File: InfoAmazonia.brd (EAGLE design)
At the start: 103.5 x 75.6 mm, 83 parts, among them IC1 ADAFRUIT FONA, IC10 TL032C, IC11 NE555, IC12 CA3140AM Z, IC13 TL081BCDG4, IC2 LM2662, IC3 74HC4051, IC4 MIC29302AWD, IC5 4050D, IC6 4053D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

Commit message: - Mudado o codigo de alguns componentes para bater com o BOM
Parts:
- IC3: value 74HC4051 -> HEF4051BT
- IC5: value 4050D -> CD4050BD
- IC6, IC7, IC8: value 4053D -> 74HC4053D
- J1, J2, J3: value BNCPTH -> 31-5431-10RFX
- JP1: value ANALOG -> 89400-0420
- JP2: value SERIAL -> 89400-0420
- JP3: value I2C -> 89400-0420
- JP4: value PWM -> 89400-0420
- MD4, MD6: value (none) -> INFO-AMAZONIA-MODULE
- R3: value 43 -> 100
- R4: value 100 -> 220
- U3: value USD-SOCKETNEW -> 10100660686
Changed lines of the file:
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@@
 <?xml version="1.0" encoding="utf-8"?>
 <!DOCTYPE eagle SYSTEM "eagle.dtd">
-<eagle version="7.3.0">
+<eagle version="7.2.0">
 <drawing>
 <settings>
@@
 </element>
 <element name="IC9" library="InfoAmazonia" package="SHT2X" value="SHT20" x="92.075" y="38.1" smashed="yes" rot="R90"/>
-<element name="J1" library="InfoAmazonia" package="BNC" value="BNCPTH" x="40.64" y="35.56" smashed="yes">
+<element name="J1" library="InfoAmazonia" package="BNC" value="31-5431-10RFX" x="40.64" y="35.56" smashed="yes">
 <attribute name="VALUE" x="34.29" y="43.18" size="0.4064" layer="27" font="vector" ratio="15" rot="SR0"/>
 </element>
@@
 <attribute name="VALUE" x="17.145" y="14.605" size="1.27" layer="27" font="vector" ratio="15" rot="R90"/>
 </element>
-<element name="R4" library="InfoAmazonia" package="R0603" value="100" x="13.97" y="10.16" smashed="yes">
+<element name="R4" library="InfoAmazonia" package="R0603" value="220" x="13.97" y="10.16" smashed="yes">
 <attribute name="NAME" x="12.85875" y="10.95375" size="1.27" layer="25" font="vector" ratio="15"/>
 <attribute name="VALUE" x="13.335" y="8.255" size="1.27" layer="27" font="vector" ratio="15"/>
 </element>
-<element name="R3" library="InfoAmazonia" package="R0603" value="43" x="10.16" y="10.16" smashed="yes">
+<element name="R3" library="InfoAmazonia" package="R0603" value="100" x="10.16" y="10.16" smashed="yes">
 <attribute name="NAME" x="9.2075" y="10.95375" size="1.27" layer="25" font="vector" ratio="15"/>
 <attribute name="VALUE" x="9.525" y="8.255" size="1.27" layer="27" font="vector" ratio="15"/>
@@
 <attribute name="VALUE" x="26.67" y="22.225" size="1.016" layer="27" font="vector" ratio="15"/>
 </element>
-<element name="U3" library="InfoAmazonia" package="MICRO-SD-SOCKET-PP" value="USD-SOCKETNEW" x="16.51" y="43.18" smashed="yes" rot="R90">
+<element name="U3" library="InfoAmazonia" package="MICRO-SD-SOCKET-PP" value="10100660686" x="16.51" y="43.18" smashed="yes" rot="R90">
 <attribute name="NAME" x="12.7" y="37.62375" size="1.778" layer="25" font="vector" ratio="15" rot="SR270"/>
 <attribute name="VALUE" x="11.43" y="34.29" size="0.8128" layer="27" font="vector" ratio="15" rot="R90"/>
 </element>
-<element name="IC5" library="InfoAmazonia" package="SO16" value="4050D" x="24.13" y="34.925" smashed="yes" rot="R270">
+<element name="IC5" library="InfoAmazonia" package="SO16" value="CD4050BD" x="24.13" y="34.925" smashed="yes" rot="R270">
 <attribute name="VALUE" x="23.495" y="38.989" size="1.27" layer="27" font="vector" ratio="15" rot="R270"/>
 <attribute name="NAME" x="24.765" y="33.655" size="1.27" layer="25" font="vector" ratio="15" rot="R90"/>
@@
 <attribute name="VALUE" x="80.645" y="71.755" size="1.27" layer="27" font="vector" ratio="15"/>
 </element>
-<element name="JP1" library="InfoAmazonia" package="JST-4-PTH-VERT" value="ANALOG" x="99.06" y="9.525" smashed="yes" rot="R270">
+<element name="JP1" library="InfoAmazonia" package="JST-4-PTH-VERT" value="89400-0420" x="99.06" y="9.525" smashed="yes" rot="R270">
 <attribute name="VALUE" x="102.06" y="8.525" size="0.4064" layer="27" rot="R270"/>
 </element>
-<element name="JP3" library="InfoAmazonia" package="JST-4-PTH-VERT" value="I2C" x="99.06" y="43.815" smashed="yes" rot="R270">
+<element name="JP3" library="InfoAmazonia" package="JST-4-PTH-VERT" value="89400-0420" x="99.06" y="43.815" smashed="yes" rot="R270">
 <attribute name="VALUE" x="102.06" y="42.815" size="0.4064" layer="27" rot="R270"/>
 </element>
-<element name="JP2" library="InfoAmazonia" package="JST-4-PTH-VERT" value="SERIAL" x="99.06" y="32.385" smashed="yes" rot="R270">
+<element name="JP2" library="InfoAmazonia" package="JST-4-PTH-VERT" value="89400-0420" x="99.06" y="32.385" smashed="yes" rot="R270">
 <attribute name="VALUE" x="102.06" y="31.385" size="0.4064" layer="27" rot="R270"/>
 </element>
-<element name="JP4" library="InfoAmazonia" package="JST-4-PTH-VERT" value="PWM" x="99.06" y="20.955" smashed="yes" rot="R270">
+<element name="JP4" library="InfoAmazonia" package="JST-4-PTH-VERT" value="89400-0420" x="99.06" y="20.955" smashed="yes" rot="R270">
 <attribute name="VALUE" x="102.06" y="19.955" size="0.4064" layer="27" rot="R270"/>
 </element>
 <element name="MD1" library="InfoAmazonia" package="INFO-AMAZONIA-MODULE" value="INFO-AMAZONIA-MODULE" x="40.64" y="20.32" rot="R270"/>
-<element name="J2" library="InfoAmazonia" package="BNC" value="BNCPTH" x="57.785" y="35.56" smashed="yes">
+<element name="J2" library="InfoAmazonia" package="BNC" value="31-5431-10RFX" x="57.785" y="35.56" smashed="yes">
 <attribute name="VALUE" x="51.435" y="43.18" size="0.4064" layer="27" rot="SR0"/>
 </element>
-<element name="J3" library="InfoAmazonia" package="BNC" value="BNCPTH" x="74.93" y="35.56" smashed="yes">
+<element name="J3" library="InfoAmazonia" package="BNC" value="31-5431-10RFX" x="74.93" y="35.56" smashed="yes">
 <attribute name="VALUE" x="68.58" y="43.18" size="0.4064" layer="27" rot="SR0"/>
 </element>
-<element name="MD4" library="InfoAmazonia" package="INFO-AMAZONIA-MODULE" value="" x="48.26" y="66.04"/>
-<element name="MD6" library="InfoAmazonia" package="INFO-AMAZONIA-MODULE" value="" x="17.78" y="66.04"/>
+<element name="MD4" library="InfoAmazonia" package="INFO-AMAZONIA-MODULE" value="INFO-AMAZONIA-MODULE" x="48.26" y="66.04"/>
+<element name="MD6" library="InfoAmazonia" package="INFO-AMAZONIA-MODULE" value="INFO-AMAZONIA-MODULE" x="17.78" y="66.04"/>
 <element name="MD5" library="InfoAmazonia" package="INFO-AMAZONIA-MODULE" value="INFO-AMAZONIA-MODULE" x="78.74" y="66.04"/>
-<element name="IC3" library="InfoAmazonia" package="SO16" value="74HC4051" x="73.025" y="18.415" smashed="yes" rot="R90">
+<element name="IC3" library="InfoAmazonia" package="SO16" value="HEF4051BT" x="73.025" y="18.415" smashed="yes" rot="R90">
 <attribute name="NAME" x="73.66" y="17.145" size="1.27" layer="25" font="vector" ratio="15" rot="R90"/>
 <attribute name="VALUE" x="75.1078" y="22.6187" size="1.016" layer="27" ratio="10" rot="R180"/>
@@
 <attribute name="VALUE" x="95.25" y="46.99" size="1.27" layer="27" rot="R90"/>
 </element>
-<element name="IC6" library="InfoAmazonia" package="SO16" value="4053D" x="38.735" y="18.415" smashed="yes" rot="R90">
+<element name="IC6" library="InfoAmazonia" package="SO16" value="74HC4053D" x="38.735" y="18.415" smashed="yes" rot="R90">
 <attribute name="VALUE" x="39.37" y="14.351" size="1.27" layer="27" ratio="10" rot="R90"/>
 <attribute name="NAME" x="39.37" y="17.145" size="1.27" layer="25" font="vector" ratio="15" rot="R90"/>
 </element>
 <element name="MD2" library="InfoAmazonia" package="INFO-AMAZONIA-MODULE" value="INFO-AMAZONIA-MODULE" x="57.785" y="20.32" rot="R270"/>
-<element name="IC7" library="InfoAmazonia" package="SO16" value="4053D" x="50.165" y="18.415" smashed="yes" rot="R90">
+<element name="IC7" library="InfoAmazonia" package="SO16" value="74HC4053D" x="50.165" y="18.415" smashed="yes" rot="R90">
 <attribute name="VALUE" x="50.8" y="14.351" size="1.27" layer="27" ratio="10" rot="R90"/>
 <attribute name="NAME" x="50.8" y="17.145" size="1.27" layer="25" font="vector" ratio="15" rot="R90"/>
 </element>
 <element name="MD3" library="InfoAmazonia" package="INFO-AMAZONIA-MODULE" value="INFO-AMAZONIA-MODULE" x="74.93" y="20.32" rot="R270"/>
-<element name="IC8" library="InfoAmazonia" package="SO16" value="4053D" x="61.595" y="18.415" smashed="yes" rot="R90">
+<element name="IC8" library="InfoAmazonia" package="SO16" value="74HC4053D" x="61.595" y="18.415" smashed="yes" rot="R90">
 <attribute name="VALUE" x="62.23" y="14.351" size="1.27" layer="27" ratio="10" rot="R90"/>
 <attribute name="NAME" x="62.23" y="17.145" size="1.27" layer="25" font="vector" ratio="15" rot="R90"/>

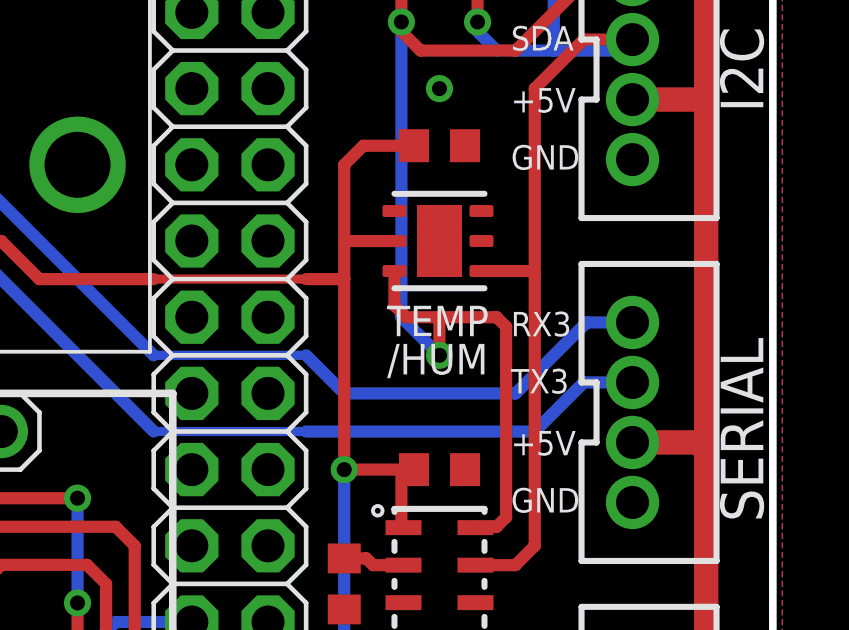
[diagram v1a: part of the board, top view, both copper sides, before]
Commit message: - Adicionado o assembly drawing
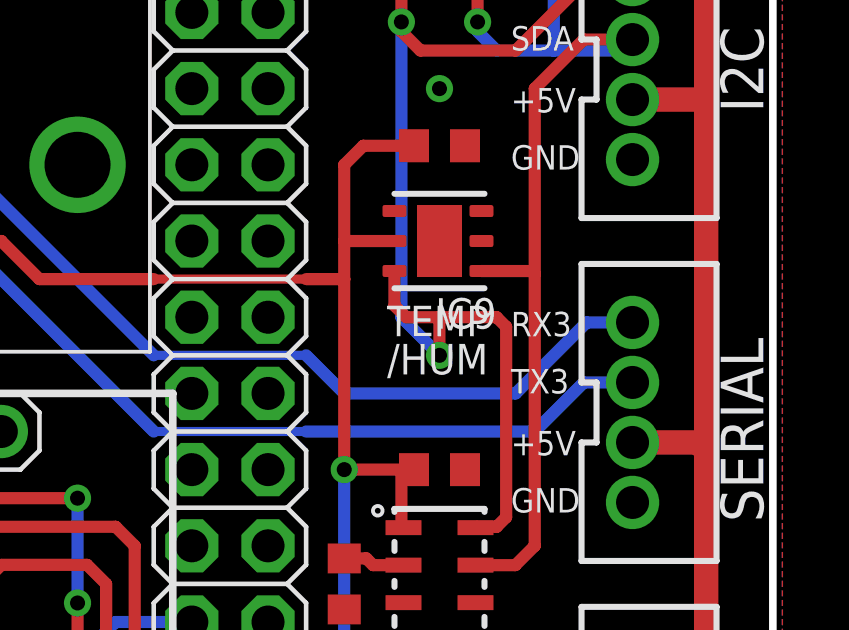
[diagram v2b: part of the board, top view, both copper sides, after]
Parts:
- IC12: value CA3140AM Z -> CA3140AMZ

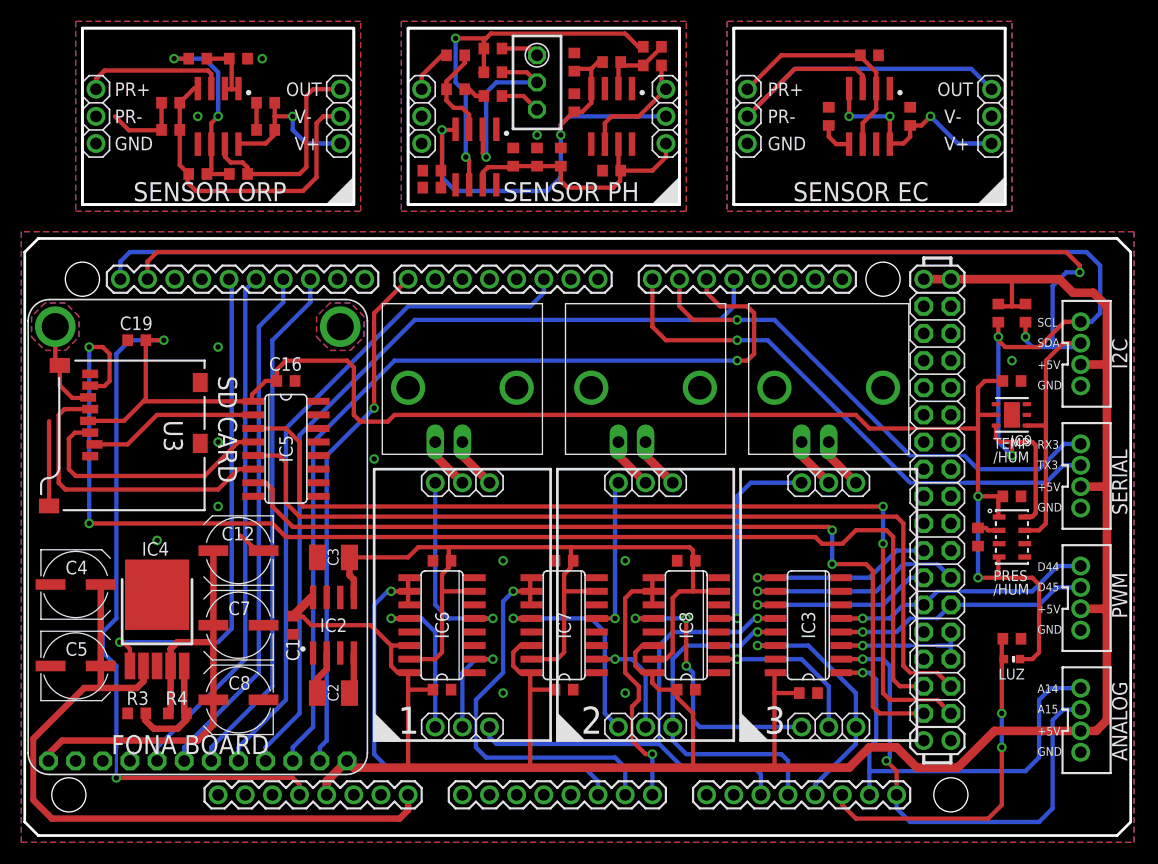
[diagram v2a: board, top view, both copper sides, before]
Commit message: - Adicionado o logo da infoamazonia nas placas
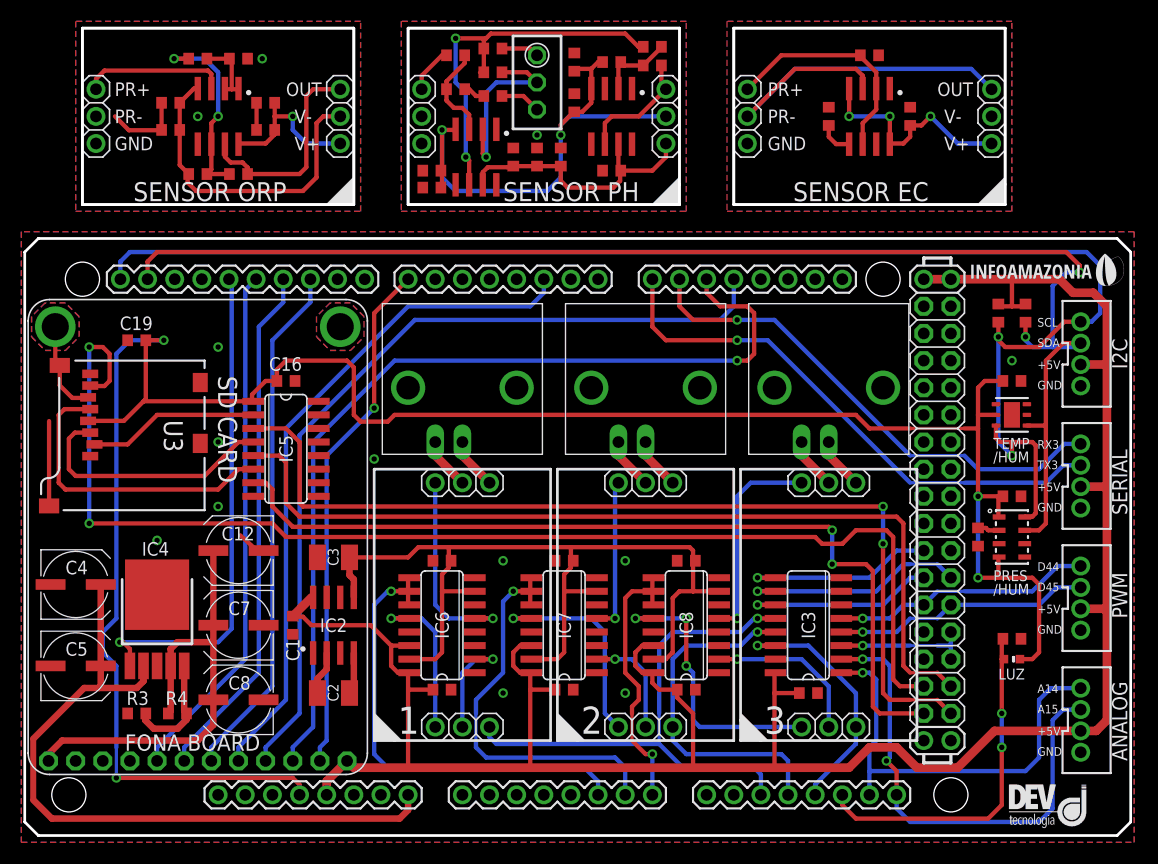
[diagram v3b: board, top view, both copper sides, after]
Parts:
- added U$1: (no value), InfoAmazonia:LOGO-INFO-0.38
- added U$2: (no value), InfoAmazonia:LOGO-DEV-0.9
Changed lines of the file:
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@@
 <setting verticaltext="up"/>
 </settings>
-<grid distance="0.025" unitdist="inch" unit="mil" style="lines" multiple="1" display="yes" altdistance="0.00625" altunitdist="inch" altunit="inch"/>
+<grid distance="0.025" unitdist="inch" unit="inch" style="lines" multiple="1" display="yes" altdistance="0.0125" altunitdist="inch" altunit="inch"/>
 <layers>
 <layer number="1" name="Top" color="4" fill="1" visible="yes" active="yes"/>
-<layer number="16" name="Bottom" color="1" fill="1" visible="no" active="yes"/>
+<layer number="16" name="Bottom" color="1" fill="1" visible="yes" active="yes"/>
 <layer number="17" name="Pads" color="2" fill="1" visible="yes" active="yes"/>
 <layer number="18" name="Vias" color="2" fill="1" visible="yes" active="yes"/>
@@
 <layer number="23" name="tOrigins" color="15" fill="1" visible="yes" active="yes"/>
 <layer number="24" name="bOrigins" color="15" fill="1" visible="no" active="yes"/>
-<layer number="25" name="tNames" color="7" fill="1" visible="no" active="yes"/>
+<layer number="25" name="tNames" color="7" fill="1" visible="yes" active="yes"/>
 <layer number="26" name="bNames" color="7" fill="1" visible="no" active="yes"/>
-<layer number="27" name="tValues" color="15" fill="1" visible="yes" active="yes"/>
+<layer number="27" name="tValues" color="15" fill="1" visible="no" active="yes"/>
 <layer number="28" name="bValues" color="7" fill="1" visible="no" active="yes"/>
 <layer number="29" name="tStop" color="7" fill="3" visible="yes" active="yes"/>
@@
 <text x="102.87" y="28.73375" size="1.4224" layer="25" font="vector" ratio="15" rot="R90">SERIAL</text>
 <text x="102.87" y="19.05" size="1.4224" layer="25" font="vector" ratio="15" rot="R90">PWM</text>
-<text x="7.77875" y="6.35" size="1.778" layer="25" font="vector" ratio="15" rot="SR0">FONA BOARD</text>
+<text x="9.04875" y="6.6675" size="1.524" layer="25" font="vector" ratio="15" rot="SR0">FONA BOARD</text>
 <text x="90.805" y="13.335" size="1.016" layer="25" font="vector" ratio="15">LUZ</text>
 <text x="90.32875" y="34.925" size="1.016" layer="25" font="vector" ratio="15">TEMP</text>
@@
 </element>
 <element name="IC9" library="InfoAmazonia" package="SHT2X" value="SHT20" x="92.075" y="38.1" smashed="yes" rot="R90">
-<attribute name="NAME" x="93.98" y="36.195" size="1.016" layer="25" font="vector" ratio="15" rot="R180"/>
 <attribute name="VALUE" x="89.8525" y="37.62375" size="1.016" layer="27" font="vector" ratio="15"/>
 </element>
@@
 <attribute name="VALUE" x="36.98875" y="11.90625" size="0.8128" layer="27" font="vector" ratio="15"/>
 </element>
+<element name="U$1" library="InfoAmazonia" package="LOGO-INFO-0.38" value="" x="88.265" y="50.165"/>
+<element name="U$2" library="InfoAmazonia" package="LOGO-DEV-0.9" value="" x="91.7575" y="-0.635"/>
 </elements>
 <signals>
